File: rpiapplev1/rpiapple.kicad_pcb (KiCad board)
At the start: 2 copper layers, 86.4 x 74.9 mm, 8 parts, among them J1 Raspberry_Pi_2_3, P1 A2Bus, U1 74HC245, U2 74HC245, U3 74HC245, U4 74HC245, U5 74HC245, U6 EMP240

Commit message: Ras Apple II
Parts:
- added D1: LED_RGB, LEDs:LED_RGB_5050-6, F.Cu at (178.1, 73.7)
- added J2: Conn_01x07, Pin_Headers:Pin_Header_Straight_1x07, F.Cu at (180.6, 86.6)
- added R1: R, Resistors_SMD:R_0603_HandSoldering, B.Cu at (179.3, 72.0)
- added R2: R, Resistors_SMD:R_0603_HandSoldering, B.Cu at (179.3, 73.7)
- added R3: R, Resistors_SMD:R_0603_HandSoldering, B.Cu at (179.3, 75.3)
- added U7: 74HC245, Housings_SOIC:SOIC-20W_7.5x12.8mm_Pitch1.27mm, B.Cu at (163.8, 118.1)
- J1, U1, U2: moved to B.Cu
- U4, U5: moved to F.Cu
- moved J1 24.1 mm to (156.2, 74.9)
- moved U1 8.03 mm to (123.2, 118.1)
- moved U5 5.68 mm to (152.4, 118.1)
- moved U6 4.19 mm to (143.1, 93.9), turned to 180 degrees
- moved U4 3.59 mm to (132.1, 118.1)
- moved U2 2.54 mm to (143.5, 118.1)
- moved U3 2.54 mm to (171.4, 118.1)
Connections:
- net Net-(P1-Pad40) renamed /PH0
- net Net-(U2-Pad9) renamed /TRW
- J1 pad 1: Net-(J1-Pad1) -> /3V3
- J1 pad 14: Net-(J1-Pad14) -> GND
- J1 pad 17: Net-(J1-Pad17) -> /3V3
- J1 pad 2: Net-(J1-Pad2) -> VCC
- J1 pad 20: Net-(J1-Pad20) -> GND
- J1 pad 25: Net-(J1-Pad25) -> GND
- J1 pad 30: Net-(J1-Pad30) -> GND
- J1 pad 34: Net-(J1-Pad34) -> GND
- J1 pad 39: Net-(J1-Pad39) -> GND
- J1 pad 4: Net-(J1-Pad4) -> VCC
- J1 pad 6: Net-(J1-Pad6) -> GND
- J1 pad 9: Net-(J1-Pad9) -> GND
- P1 pad 20: Net-(P1-Pad20) -> /IOSTRB
- P1 pad 23: /INT -> /INT0
- P1 pad 28: /INT -> /INTI
- P1 pad 36: Net-(P1-Pad36) -> /7M
- U1 pad 1: Net-(U1-Pad1) -> /TWR
- U1 pad 11: /D0 -> /D7
- U1 pad 12: /D1 -> /D6
- U1 pad 13: /D2 -> /D5
- U1 pad 14: /D3 -> /D4
- U1 pad 15: /D4 -> /D3
- U1 pad 16: /D5 -> /D2
- U1 pad 17: /D6 -> /D1
- U1 pad 18: /D7 -> /D0
- U1 pad 19: Net-(U1-Pad19) -> GND
- U1 pad 2: Net-(U1-Pad2) -> /TD0
- U1 pad 3: Net-(U1-Pad3) -> /TD1
- U1 pad 4: Net-(U1-Pad4) -> /TD2
- U1 pad 5: Net-(U1-Pad5) -> /TD3
- U1 pad 6: Net-(U1-Pad6) -> /TD4
- U1 pad 7: Net-(U1-Pad7) -> /TD5
- U1 pad 8: Net-(U1-Pad8) -> /TD6
- U1 pad 9: Net-(U1-Pad9) -> /TD7
- U2 pad 1: Net-(U2-Pad1) -> /TDIR
- U2 pad 11: Net-(U2-Pad11) -> /RW
- U2 pad 19: Net-(U2-Pad19) -> GND
- U3 pad 1: Net-(U3-Pad1) -> GND
- U3 pad 11: Net-(U3-Pad11) -> /IOSEL
- U3 pad 12: Net-(U3-Pad12) -> /IOSTRB
- U3 pad 13: Net-(U3-Pad13) -> /DEVSEL
- U3 pad 14: Net-(U3-Pad14) -> /PH1
- U3 pad 15: Net-(U3-Pad15) -> /7M
- U3 pad 16: Net-(U3-Pad16) -> /INTI
- U3 pad 17: Net-(U3-Pad17) -> /DMAI
- U3 pad 19: Net-(U3-Pad19) -> GND
- U3 pad 3: Net-(U3-Pad3) -> /TDMAI
- U3 pad 4: Net-(U3-Pad4) -> /TINTI
- U3 pad 5: Net-(U3-Pad5) -> /T7M
- U3 pad 6: Net-(U3-Pad6) -> /TPH1
- U3 pad 7: Net-(U3-Pad7) -> /TDEVSEL
- U3 pad 8: Net-(U3-Pad8) -> /TIOSTRB
- U3 pad 9: Net-(U3-Pad9) -> /TIOSEL
- U4 pad 1: Net-(U4-Pad1) -> /TDIR
- U4 pad 11: /A7 -> /A0
- U4 pad 12: /A6 -> /A1
- U4 pad 13: /A5 -> /A2
- U4 pad 14: /A4 -> /A3
- U4 pad 15: /A3 -> /A4
- U4 pad 16: /A2 -> /A5
- U4 pad 17: /A1 -> /A6
- U4 pad 18: /A0 -> /A7
- U4 pad 19: Net-(U4-Pad19) -> GND
- U4 pad 2: Net-(U4-Pad2) -> /TA7
- U4 pad 3: Net-(U4-Pad3) -> /TA6
- U4 pad 4: Net-(U4-Pad4) -> /TA5
- U4 pad 5: Net-(U4-Pad5) -> /TA4
- U4 pad 6: Net-(U4-Pad6) -> /TA3
- U4 pad 7: Net-(U4-Pad7) -> /TA2
- U4 pad 8: Net-(U4-Pad8) -> /TA1
- U4 pad 9: Net-(U4-Pad9) -> /TA0
- U5 pad 1: Net-(U5-Pad1) -> /TDIR
- U5 pad 11: /A15 -> /A8
- U5 pad 12: /A14 -> /A9
- U5 pad 13: /A13 -> /A10
- U5 pad 14: /A12 -> /A11
- U5 pad 15: /A11 -> /A12
- U5 pad 16: /A10 -> /A13
- U5 pad 17: /A9 -> /A14
- U5 pad 18: /A8 -> /A15
- U5 pad 19: Net-(U5-Pad19) -> GND
- U5 pad 2: Net-(U5-Pad2) -> /TA15
- U5 pad 3: Net-(U5-Pad3) -> /TA14
- U5 pad 4: Net-(U5-Pad4) -> /TA13
- U5 pad 5: Net-(U5-Pad5) -> /TA12
- U5 pad 6: Net-(U5-Pad6) -> /TA11
- U5 pad 7: Net-(U5-Pad7) -> /TA10
- U5 pad 8: Net-(U5-Pad8) -> /TA9
- U5 pad 9: Net-(U5-Pad9) -> /TA8
- U6 pad 12: Net-(U6-Pad12) -> /RC4
- U6 pad 15: Net-(U6-Pad15) -> /TIOSTRB
- U6 pad 16: Net-(U6-Pad16) -> /TDEVSEL
- U6 pad 17: Net-(U6-Pad17) -> /TINTI
- U6 pad 18: Net-(U6-Pad18) -> /TDMAI
- U6 pad 19: Net-(U6-Pad19) -> /LED1
- U6 pad 20: Net-(U6-Pad20) -> /LED2
- U6 pad 21: Net-(U6-Pad21) -> /LED3
- U6 pad 22: Net-(U6-Pad22) -> /TMS
- U6 pad 23: Net-(U6-Pad23) -> /TDI
- U6 pad 24: Net-(U6-Pad24) -> /TCK
- U6 pad 26: Net-(U6-Pad26) -> /RD2
- U6 pad 27: Net-(U6-Pad27) -> /RD3
- U6 pad 28: Net-(U6-Pad28) -> /RA6
- U6 pad 29: Net-(U6-Pad29) -> /RD4
- U6 pad 30: Net-(U6-Pad30) -> /RA7
- U6 pad 31: Net-(U6-Pad31) -> /3V3
- U6 pad 32: Net-(U6-Pad32) -> /RC2
- U6 pad 33: Net-(U6-Pad33) -> /RC1
- U6 pad 34: Net-(U6-Pad34) -> /RC11
- U6 pad 35: Net-(U6-Pad35) -> /RC7
- U6 pad 36: Net-(U6-Pad36) -> /RC6
- U6 pad 37: Net-(U6-Pad37) -> /RC8
- U6 pad 38: Net-(U6-Pad38) -> /RA2
- U6 pad 39: Net-(U6-Pad39) -> /RC9
- U6 pad 40: Net-(U6-Pad40) -> /RA1
- U6 pad 41: Net-(U6-Pad41) -> /RA0
- U6 pad 42: Net-(U6-Pad42) -> /RA3
- U6 pad 43: Net-(U6-Pad43) -> /RD7
- U6 pad 44: Net-(U6-Pad44) -> /RD1
- U6 pad 45: Net-(U6-Pad45) -> /3V3
- U6 pad 46: Net-(U6-Pad46) -> /RD0
- U6 pad 47: Net-(U6-Pad47) -> /RD5
- U6 pad 48: Net-(U6-Pad48) -> /RA4
- U6 pad 49: Net-(U6-Pad49) -> /RD6
- U6 pad 50: Net-(U6-Pad50) -> /RA5
- U6 pad 51: Net-(U6-Pad51) -> /RC0
- U6 pad 52: Net-(U6-Pad52) -> /RC3
- U6 pad 53: Net-(U6-Pad53) -> /RC4
- U6 pad 54: Net-(U6-Pad54) -> /RC10
- U6 pad 55: Net-(U6-Pad55) -> /RC5
- U6 pad 58: Net-(U6-Pad58) -> /TDIR
- U6 pad 59: Net-(U6-Pad59) -> /3V3
- U6 pad 60: Net-(U6-Pad60) -> /TIOSEL
- U6 pad 61: Net-(U6-Pad61) -> /TA0
- U6 pad 62: Net-(U6-Pad62) -> /TD0
- U6 pad 63: Net-(U6-Pad63) -> /3V3
- U6 pad 64: Net-(U6-Pad64) -> /TA1
- U6 pad 65: Net-(U6-Pad65) -> /TD1
- U6 pad 66: Net-(U6-Pad66) -> /TA2
- U6 pad 67: Net-(U6-Pad67) -> /TD2
- U6 pad 68: Net-(U6-Pad68) -> /TA3
- U6 pad 69: Net-(U6-Pad69) -> /TD3
- U6 pad 70: Net-(U6-Pad70) -> /TA4
- U6 pad 71: Net-(U6-Pad71) -> /TD4
- U6 pad 72: Net-(U6-Pad72) -> /TA5
- U6 pad 73: Net-(U6-Pad73) -> /TD5
- U6 pad 74: Net-(U6-Pad74) -> /TA6
- U6 pad 75: Net-(U6-Pad75) -> /TD6
- U6 pad 76: Net-(U6-Pad76) -> /TA7
- U6 pad 77: Net-(U6-Pad77) -> /TD7
- U6 pad 78: Net-(U6-Pad78) -> /TA8
- U6 pad 79: Net-(U6-Pad79) -> /TA9
- U6 pad 80: Net-(U6-Pad80) -> /3V3
- U6 pad 81: Net-(U6-Pad81) -> /TA10
- U6 pad 82: Net-(U6-Pad82) -> /TA11
- U6 pad 83: Net-(U6-Pad83) -> /TPH1
- U6 pad 84: Net-(U6-Pad84) -> /TA12
- U6 pad 85: Net-(U6-Pad85) -> /TA13
- U6 pad 86: Net-(U6-Pad86) -> /T7M
- U6 pad 87: Net-(U6-Pad87) -> /TA14
- U6 pad 88: Net-(U6-Pad88) -> /TA15
- U6 pad 89: Net-(U6-Pad89) -> /TWR
- U6 pad 9: Net-(U6-Pad9) -> /3V3
- U6 pad 90: Net-(U6-Pad90) -> /TINH
- U6 pad 91: Net-(U6-Pad91) -> /TRES
- U6 pad 92: Net-(U6-Pad92) -> /TIRQ
- U6 pad 93: Net-(U6-Pad93) -> /TDIR2
- U6 pad 95: Net-(U6-Pad95) -> /TNMI
- U6 pad 96: Net-(U6-Pad96) -> /TRDY
- U6 pad 97: Net-(U6-Pad97) -> /TDMA
- U6 pad 98: Net-(U6-Pad98) -> /TDMAO
- U6 pad 99: Net-(U6-Pad99) -> /TINTO
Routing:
- net GND: track 0.00 -> 382.8 mm, vias 0 -> 25
- net VCC: track 0.00 -> 150.8 mm, vias 0 -> 2
- net /3V3: track 0.00 -> 129.2 mm, vias 0 -> 3
- net /TDIR: track 0.00 -> 66.9 mm, vias 0 -> 1
- net /IOSEL: track 0.00 -> 66.7 mm
- net /LED1: track 0.00 -> 63.6 mm
- net /RC4: track 0.00 -> 50.2 mm
- net /LED2: track 0.00 -> 42.6 mm
- net /TPH1: track 0.00 -> 41.9 mm
- net /TIOSEL: track 0.00 -> 41.7 mm, vias 0 -> 2
- net /T7M: track 0.00 -> 41.3 mm
- net /TDI: track 0.00 -> 39.6 mm
- net /TWR: track 0.00 -> 38.8 mm, vias 0 -> 1
- net /DEVSEL: track 0.00 -> 37.8 mm, vias 0 -> 1
- net /RC5: track 0.00 -> 35.9 mm
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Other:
- board size 86.4 x 74.9 mm -> 81.3 x 74.9 mm
- board text added: "2018.03.23"
- board text added: "74HC245"
- board text added: "RAS APPLE II"
- board text added: "TCK GND TDO 3V3 TMS TDI GND"
- board text added: "meeso.kim@gmail.com"

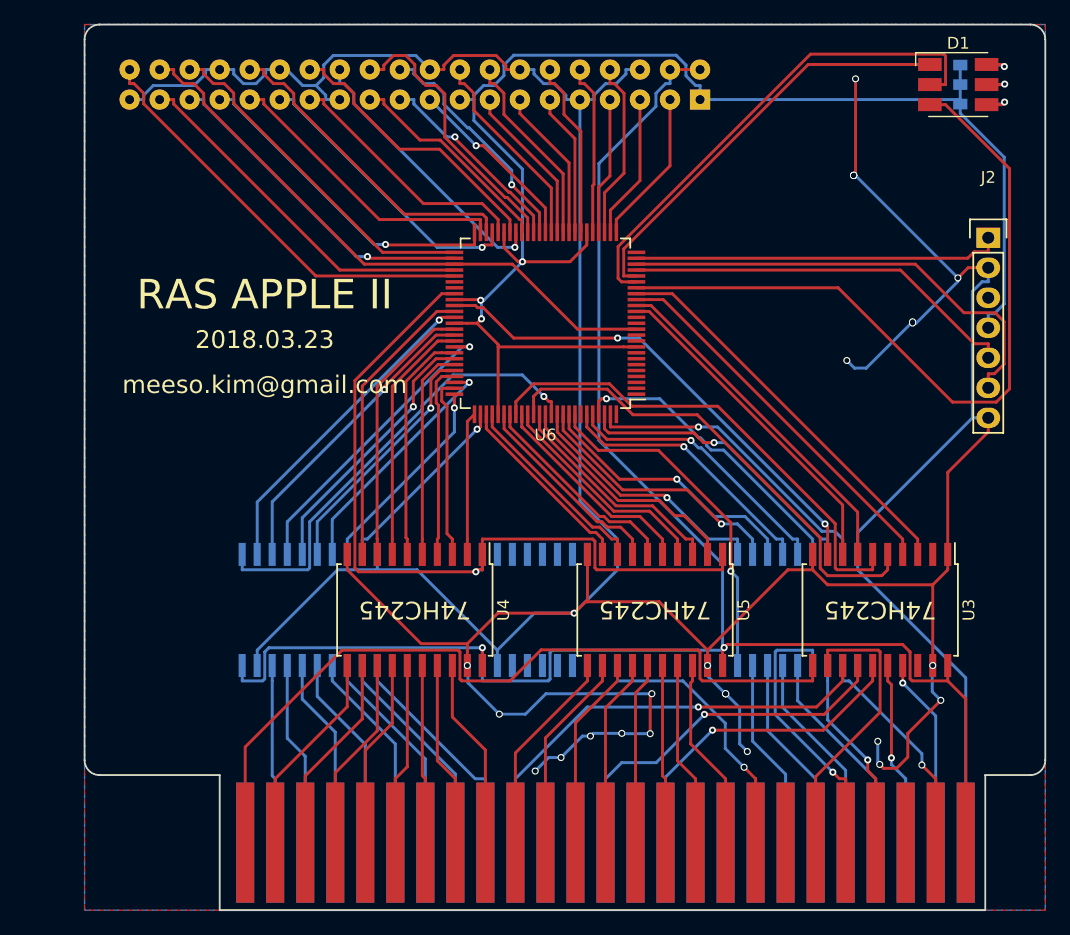
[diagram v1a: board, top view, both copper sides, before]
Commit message: update for RPIZ80, RPIAPPLE, RPMSXP
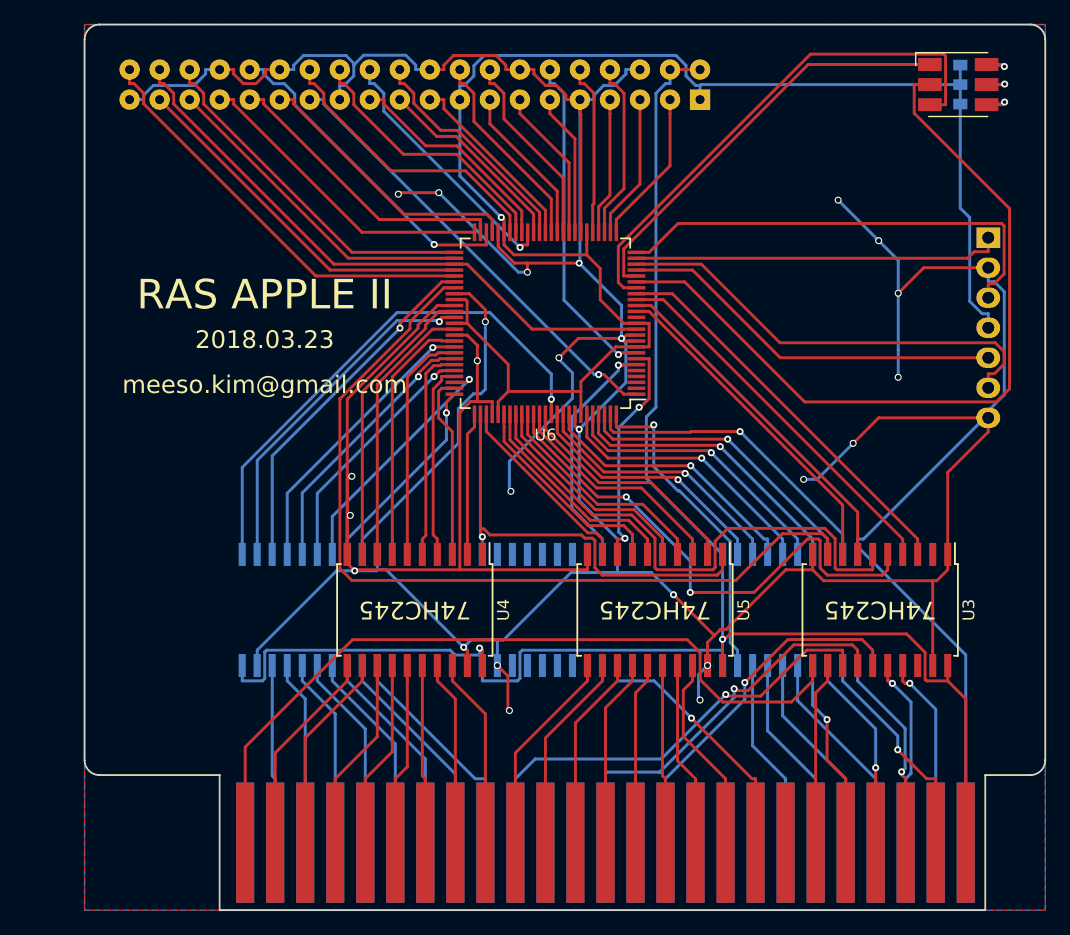
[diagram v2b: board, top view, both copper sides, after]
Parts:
- J2: moved to B.Cu
- turned J2 to 180 degrees
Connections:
- net /PH0 renamed Net-(P1-Pad40)
- U6 pad 1: Net-(U6-Pad1) -> /RD0
- U6 pad 10: Net-(U6-Pad10) -> GND
- U6 pad 100: Net-(U6-Pad100) -> /TDIR2
- U6 pad 11: Net-(U6-Pad11) -> GND
- U6 pad 13: Net-(U6-Pad13) -> /3V3
- U6 pad 25: Net-(U6-Pad25) -> /TDO
- U6 pad 32: /RC2 -> GND
- U6 pad 46: /RD0 -> GND
- U6 pad 56: Net-(U6-Pad56) -> /TD1
- U6 pad 57: Net-(U6-Pad57) -> /TIOSEL
- U6 pad 58: /TDIR -> /TD7
- U6 pad 6: Net-(U6-Pad6) -> /TRW
- U6 pad 60: /TIOSEL -> GND
- U6 pad 65: /TD1 -> GND
- U6 pad 7: Net-(U6-Pad7) -> /TA9
- U6 pad 77: /TD7 -> /TDIR
- U6 pad 79: /TA9 -> GND
- U6 pad 8: Net-(U6-Pad8) -> /RC2
- U6 pad 93: /TDIR2 -> GND
- U6 pad 94: Net-(U6-Pad94) -> /3V3
- U7 pad 11: /INTO -> /INT0
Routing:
- net GND: track 382.8 -> 457.5 mm, vias 25 -> 24
- net /TDO: track 0.00 -> 39.1 mm
- net /TIOSEL: track 41.7 -> 73.1 mm, vias 2 -> 0
- net /TDIR: track 66.9 -> 40.0 mm
- net /LED2: track 42.6 -> 66.6 mm
- net /TRW: track 0.00 -> 20.3 mm, vias 0 -> 1
- net /LED1: track 63.6 -> 44.7 mm
- net /INT0: track 0.00 -> 16.9 mm, vias 0 -> 1
- net /RD0: track 21.4 -> 38.2 mm, vias 0 -> 1
- net /RC2: track 15.1 -> 28.3 mm, vias 0 -> 1
- net /TD7: track 16.3 -> 28.6 mm
- net /IOSTRB: track 24.2 -> 15.4 mm
- net /RDY: track 23.4 -> 16.1 mm
- net /RW: track 28.5 -> 21.8 mm
- net /3V3: track 129.2 -> 135.2 mm, vias 3 -> 1
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
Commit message: PCB files for order
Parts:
- added C1: C, Capacitors_SMD:C_0603_HandSoldering, F.Cu at (179.6, 118.4)
- added C2: C, Capacitors_SMD:C_0603_HandSoldering, B.Cu at (155.7, 117.9)
- added C3: C, Capacitors_SMD:C_0603_HandSoldering, F.Cu at (160.8, 117.9)
- added C4: C, Capacitors_SMD:C_0603_HandSoldering, F.Cu at (140.2, 118.1)
- added C5: C, Capacitors_SMD:C_0603_HandSoldering, B.Cu at (135.4, 118.1)
- added C6: C, Capacitors_SMD:C_0603_HandSoldering, B.Cu at (114.6, 117.9)
- added C7: C, Capacitors_SMD:C_0603_HandSoldering, B.Cu at (145.8, 91.2)
- added R4: R, Resistors_SMD:R_0603_HandSoldering, F.Cu at (170.7, 126.2)
- added R5: R, Resistors_SMD:R_0603_HandSoldering, F.Cu at (170.7, 128.3)
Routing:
- net /3V3: track 135.2 -> 207.3 mm
- net GND: track 457.5 -> 403.4 mm, vias 24 -> 4
- net VCC: track 147.9 -> 187.7 mm, vias 2 -> 1
- net /TIOSEL: track 73.1 -> 42.6 mm, vias 0 -> 2
- net /TA9: track 19.6 -> 34.0 mm, vias 2 -> 0
- net /LED1: track 44.7 -> 31.4 mm, vias 0 -> 2
- net /IOSTRB: track 15.4 -> 28.0 mm
- net /TWR: track 44.5 -> 36.1 mm
- net /7M: track 30.3 -> 27.7 mm
- net /TD7: track 28.6 -> 26.2 mm
- net /TRW: track 20.3 -> 18.0 mm
- net /TPH1: track 45.3 -> 43.2 mm, vias 0 -> 2
- net /INT0: track 16.9 -> 18.7 mm
- net /DMAI: track 16.4 -> 18.0 mm
- net /DMAO: track 18.7 -> 20.2 mm
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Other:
- board text added: "EPM240"
